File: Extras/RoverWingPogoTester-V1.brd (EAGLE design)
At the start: 81.3 x 81.3 mm, 10 parts

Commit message: Pogo Tester design finished
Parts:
- removed FRAME1, FRAME2: FRAME-LETTERNO_PACKAGE, SparkFun-Aesthetics:DUMMY
- added ANALOGGND, ANALOGPOWER, ANALOGSIG: (no value), SparkFun:1X06
- added D1, D2, D3, D4, D5, D6, D7: LTL-1CHG, LED:RADIAL_3MM
- added ENCODER1, ENCODER1OUT, ENCODER2, ENCODER2OUT, SONAR1, SONAR1OUT, SONAR2, SONAR2OUT, SONAR3, SONAR3OUT: 62000411121, Headers:62000411121
- added FRAME3: FRAME-LETTERNO_PACKAGE, RoverWing-V1.5:DUMMY
- added GND, MOTOR1A, MOTOR1B, MOTOR2A, MOTOR2B, SCL, SDA, VIN: M01PTH, SparkFun:1X01
- added J14: DF13-4P-1.25DSA, RoverWing-V1.5:DF13-4P-1.25DSA
- added J15: DF13-6P-1.25DSA, RoverWing-V1.5:DF13-6P-1.25DSA
- added J17: HEADER-3X04, RoverWing-V1.5:3X04
- added J18, J19, J20, J21: 62000311121, Headers:62000311121
- added J23: HEADER-2X12, RoverWing-V1.5:2X12
- added J24: HEADER-2X16, RoverWing-V1.5:2X16
- added J25: XT60-M, XT60-M:AMASS_XT60-M
- added LEDRESISTOR, TESTER, VOLTAGE_DIVIDER: 10k, SparkFun-Resistors:AXIAL-0.3
- added MOTOR1OUT, MOTOR2OUT: B2P-VH(LF)(SN), Connectors:HDR-02
- added PAD1, PAD2, PAD3, PAD4, PAD5: (no value), wirepad:2,15/1,0
- added U$1: SAMTEC-FTSH-105-01-X-D-RAJ, SAMTEC-FTSH-105-01-X-D-RA:SAMTEC-FTSH-105-01-X-D-RA
- added U$11, U$13, U$17: FIDUCIAL, RoverWing-V1.5:FIDUCIAL_1MM
- U$14, U$15, U$24, U$25, U$26, U$27, U$3, U$4: device CrickitCopy:MOUNTINGHOLE_3.0_NPH -> RoverWing-V1.5:MOUNTINGHOLE_3.0_NPH
- moved U$15 98.2 mm to (-36.1, -82.1)
- moved U$25 98.2 mm to (39.4, -82.1)
- moved U$14 98.2 mm to (-36.1, -114.4)
- moved U$24 98.2 mm to (39.4, -114.4)
- moved U$26 98.2 mm to (-14.5, -60.5)
- moved U$27 98.2 mm to (17.8, -60.5)
- moved U$3 98.2 mm to (-14.5, -136.0)
- moved U$4 98.2 mm to (17.8, -136.0)
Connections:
- new net !RESET1: J24.1, J24.2
- new net 11: ENCODER1.1, ENCODER1OUT.1
- new net 12: ENCODER1.2, ENCODER1OUT.2
- new net 13: ENCODER1.3, ENCODER1OUT.3
- new net 14: ENCODER1.4, ENCODER1OUT.4
- new net 21: ENCODER2.1, ENCODER2OUT.1
- new net 22: ENCODER2.2, ENCODER2OUT.2
- new net 23: ENCODER2.3, ENCODER2OUT.3
- new net 24: ENCODER2.4, ENCODER2OUT.4
- new net 3.3V: J24.3, J24.4, PAD5.1, U$1.10
- new net 5V: J14.P$1, J15.P$1, J17.11, J17.2, J17.5, J17.8, J18.2, J19.2, J20.2, J21.2, J23.5, J23.6
- new net D10: D6.A, J23.10, J23.9
- new net D11: D7.A, J23.7, J23.8
- new net D5: D1.A, J23.19, J23.20
- new net D6: D2.A, J23.17, J23.18
- new net D7: D3.A, J23.15, J23.16
- new net D8: D4.A, J23.13, J23.14
- new net D9: D5.A, J23.11, J23.12
- new net GND: GND.1, J14.P$4, J15.P$6, J17.12, J17.3, J17.6, J17.9, J18.1, J19.1, J20.1, J21.1, J24.7, J24.8, J25.2, LEDRESISTOR.P$1, PAD4.1, U$1.6, U$1.8
- new net LEDGND: D1.C, D2.C, D3.C, D4.C, D5.C, D6.C, D7.C, LEDRESISTOR.P$2
- new net N$1: MOTOR1A.1, MOTOR1OUT.2
- new net N$10: SONAR2.4, SONAR2OUT.4
- new net N$11: SONAR2.3, SONAR2OUT.3
- new net N$12: SONAR2.2, SONAR2OUT.2
- new net N$13: SONAR2.1, SONAR2OUT.1
- new net N$14: SONAR3.4, SONAR3OUT.4
- new net N$15: SONAR3.3, SONAR3OUT.3
- new net N$16: SONAR3.2, SONAR3OUT.2
- new net N$17: SONAR3.1, SONAR3OUT.1
- new net N$18: ANALOGSIG.1, ANALOGSIG.2, ANALOGSIG.3, ANALOGSIG.4, ANALOGSIG.5, ANALOGSIG.6, TESTER.P$1, VOLTAGE_DIVIDER.P$2
- new net N$2: MOTOR1B.1, MOTOR1OUT.1
- new net N$23: ANALOGGND.1, ANALOGGND.2, ANALOGGND.3, ANALOGGND.4, ANALOGGND.5, ANALOGGND.6, VOLTAGE_DIVIDER.P$1
- new net N$24: J23.3, J23.4
- new net N$26: J15.P$4
- new net N$27: J15.P$5
- new net N$3: MOTOR2A.1, MOTOR2OUT.2
- new net N$34: J24.5, J24.6
- new net N$35: J24.10, J24.9
- new net N$36: J24.11, J24.12
- new net N$37: J24.13, J24.14
- new net N$38: J24.15, J24.16
- new net N$39: J24.17, J24.18
- new net N$4: MOTOR2B.1, MOTOR2OUT.1
- new net N$47: J24.19, J24.20
- new net N$5: SONAR1.4, SONAR1OUT.4
- new net N$6: SONAR1.3, SONAR1OUT.3
- new net N$60: J24.21, J24.22
- new net N$61: J24.23, J24.24
- new net N$62: J24.25, J24.26
- new net N$63: J24.27, J24.28
- new net N$64: J24.29, J24.30
- new net N$65: J24.31, J24.32
- new net N$7: SONAR1.2, SONAR1OUT.2
- new net N$8: ANALOGPOWER.1, ANALOGPOWER.2, ANALOGPOWER.3, ANALOGPOWER.4, ANALOGPOWER.5, ANALOGPOWER.6, TESTER.P$2
- new net N$9: SONAR1.1, SONAR1OUT.1
- new net RESET: PAD1.1, U$1.1
- new net RX: J15.P$3
- new net SCL1: J23.21, J23.22, SCL.1
- new net SCL2: J14.P$2
- new net SDA1: J23.23, J23.24, SDA.1
- new net SDA2: J14.P$3
- new net SERVO1: J17.1, J20.3
- new net SERVO2: J17.4, J18.3
- new net SERVO3: J17.7, J19.3
- new net SERVO4: J17.10, J21.3
- new net SWCLK: PAD2.1, U$1.7
- new net SWDIO: PAD3.1, U$1.9
- new net TX: J15.P$2
- new net VIN: J23.1, J23.2, J25.1, VIN.1
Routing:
- net GND: track 0.00 -> 494.9 mm
- net VIN: track 0.00 -> 167.1 mm
- net 3.3V: track 0.00 -> 164.1 mm
- net 5V: track 0.00 -> 152.0 mm
- net N$2: track 0.00 -> 138.6 mm
- net N$1: track 0.00 -> 133.8 mm
- net 14: track 0.00 -> 102.8 mm
- net 13: track 0.00 -> 101.2 mm
- net 12: track 0.00 -> 99.5 mm
- net 11: track 0.00 -> 97.9 mm
- net SERVO2: track 0.00 -> 80.7 mm
- net SERVO3: track 0.00 -> 77.9 mm
- net N$4: track 0.00 -> 73.9 mm
- net N$3: track 0.00 -> 72.0 mm
- net SWCLK: track 0.00 -> 69.7 mm
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- removed copper zone on layer 1, net GND
- removed copper zone on layer 16, net GND
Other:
- board size 81.3 x 81.3 mm -> 108 x 160 mm
- board text added: "+"
- board text added: "1"
- board text added: "2"
- board text added: "3"
- board text added: "3.3V"
- board text added: "4"
- board text added: "5V"
- board text added: "A"
- board text added: "A1"
- board text added: "A2"
- board text added: "A3"
- board text added: "A4"
- board text added: "A5"
- board text added: "A6"
- board text added: "ANALOG"
- board text added: "B"
- board text added: "COMPASS"
- board text added: "DATA"
- board text added: "ECHO"
- board text added: "GND"
- board text added: "GPS"
- board text added: "I2C"
- board text added: "MOTOR1"
- board text added: "MOTOR2"
- board text added: "NEOPIXEL"
- board text added: "RESET"
- board text added: "RX"
- board text added: "RoverWing V2.2 D. Bershadsky, A. Kirillov github.com/roverwing"
- board text added: "SCL"
- board text added: "SDA"
- board text added: "SERVO"
- board text added: "SIGNAL"
- board text added: "SONAR1"
- board text added: "SONAR2"
- board text added: "SONAR3"
- board text added: "TRIG"
- board text added: "TX"

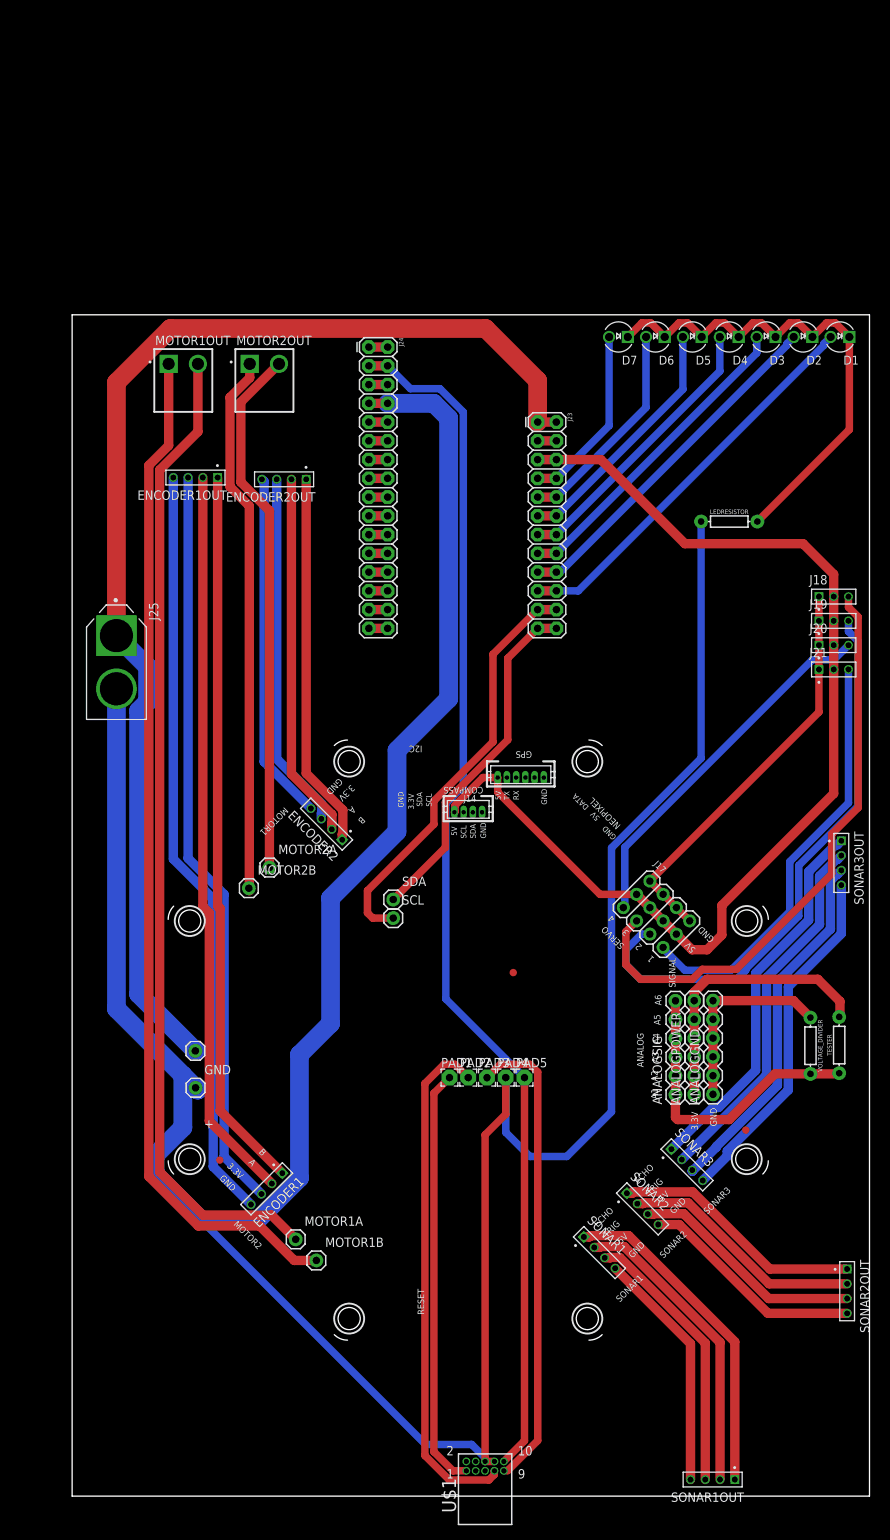
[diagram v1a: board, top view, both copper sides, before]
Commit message: Finished Pogo Tester Design
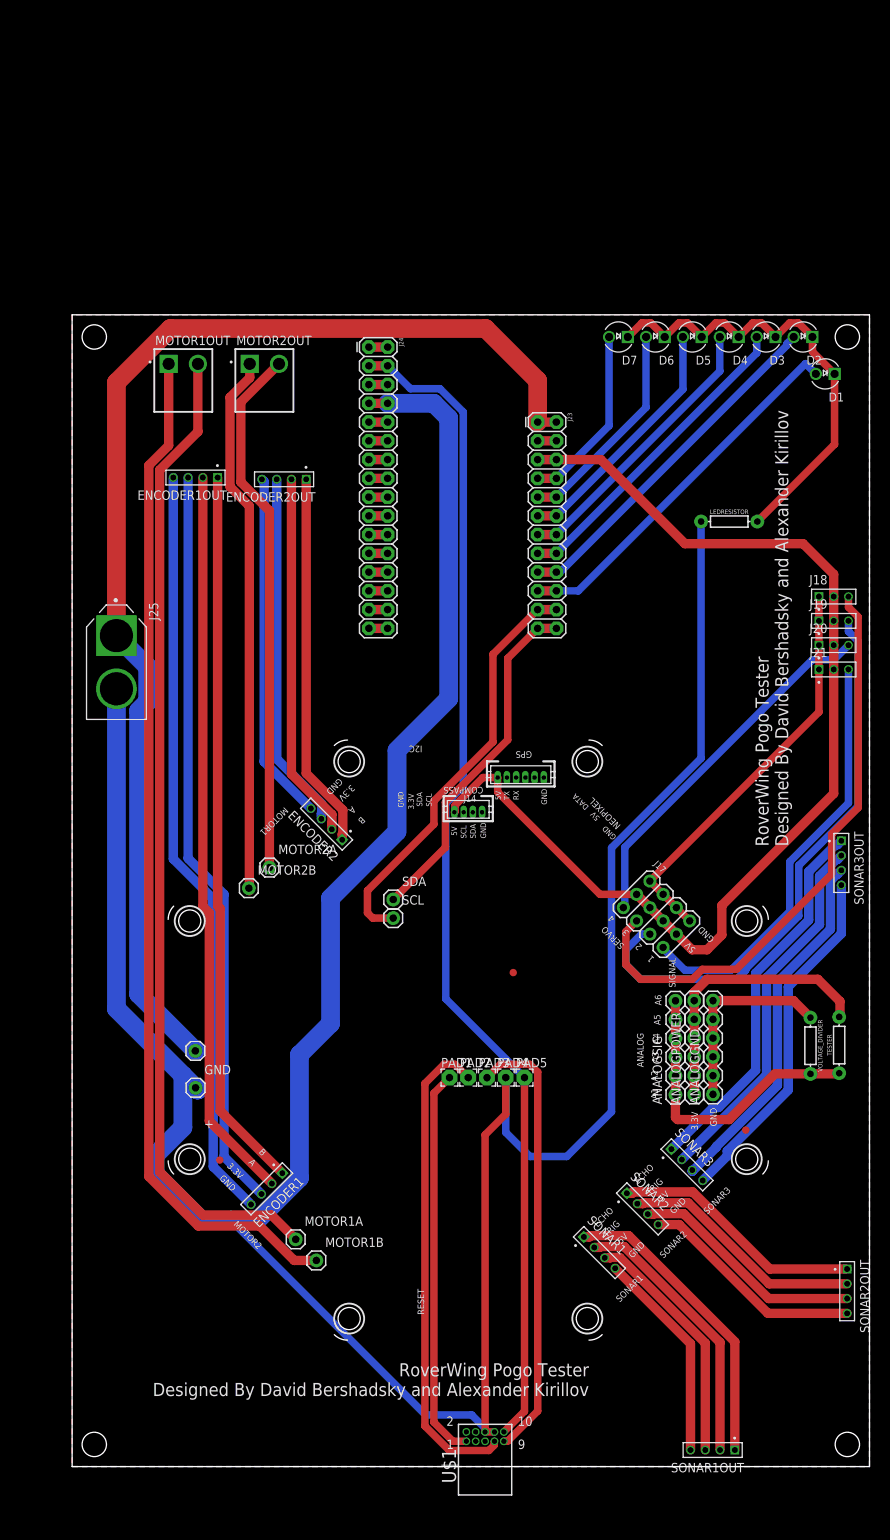
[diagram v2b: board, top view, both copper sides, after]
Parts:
- moved D1 5.39 mm to (50.0, -8.00)
- moved SONAR1OUT 4.00 mm to (34.8, -153.8)
- moved U$1 4.00 mm to (3.93, -155.1)
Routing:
- net GND: track 494.9 -> 485.2 mm
- net LEDGND: track 69.6 -> 63.5 mm
- net SWCLK: track 69.7 -> 65.7 mm
- net RESET: track 57.0 -> 53.0 mm
- net N$9: track 45.1 -> 41.1 mm
- net N$7: track 41.0 -> 37.0 mm
- net N$6: track 36.9 -> 32.9 mm
- net 3.3V: track 164.1 -> 160.1 mm
- net N$5: track 32.8 -> 28.8 mm
- net SWDIO: track 64.2 -> 60.2 mm
- net D5: track 54.0 -> 51.0 mm
- added copper zone on layer 1, net GND
- added copper zone on layer 16, net GND
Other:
- board size 108 x 160 mm -> 108 x 156 mm
- board text added: "RoverWing Pogo Tester Designed By David Bershadsky and Alexander Kirillov"
